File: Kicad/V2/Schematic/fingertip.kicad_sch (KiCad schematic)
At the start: 1 part

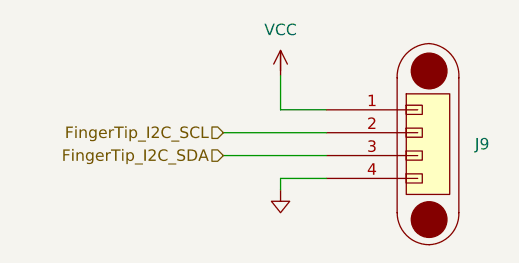
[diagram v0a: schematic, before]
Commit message: New footprints : Ferrite bead, poly fuse, TVS diode. To do: FPC connector footprint
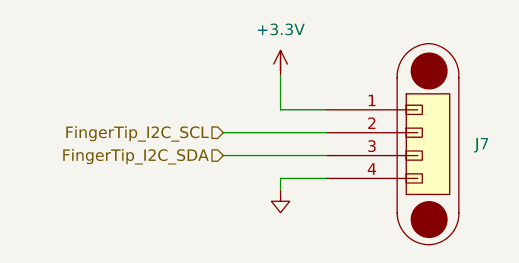
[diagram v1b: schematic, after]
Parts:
- renumbered J9 to J7
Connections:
- net VCC renamed +3.3V
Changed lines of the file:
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@@
 		(dnp no)
 		(fields_autoplaced yes)
-		(property "Reference" "GND039"
+		(property "Reference" "GND041"
 			(at 130.81 100.076 0)
 			(hide yes)
@@
 			(project "G-Love"
 				(path "/808bc5ea-49ac-4454-ba77-8b20d01ce159/8701d982-557e-4c73-bfaa-5f02d2e6c25d"
-					(reference "GND039")
+					(reference "GND041")
+					(unit 1)
+				)
+			)
+		)
+	)
+	(symbol
+		(lib_id "G-Love:+3.3V")
+		(at 130.81 82.55 0)
+		(unit 1)
+		(body_style 1)
+		(exclude_from_sim no)
+		(in_bom no)
+		(on_board no)
+		(in_pos_files yes)
+		(dnp no)
+		(fields_autoplaced yes)
+		(property "Reference" "#PWR024"
+			(at 134.62 84.328 0)
+			(hide yes)
+			(show_name no)
+			(do_not_autoplace no)
+			(effects
+				(font
+					(size 1.27 1.27)
+				)
+			)
+		)
+		(property "Value" "+3.3V"
+			(at 130.81 78.74 0)
+			(show_name no)
+			(do_not_autoplace no)
+			(effects
+				(font
+					(size 1.27 1.27)
+				)
+			)
+		)
+		(property "Footprint" ""
+			(at 130.81 82.55 0)
+			(hide yes)
+			(show_name no)
+			(do_not_autoplace no)
+			(effects
+				(font
+					(size 1.27 1.27)
+				)
+			)
+		)
+		(property "Datasheet" ""
+			(at 130.81 82.55 0)
+			(hide yes)
+			(show_name no)
+			(do_not_autoplace no)
+			(effects
+				(font
+					(size 1.27 1.27)
+				)
+			)
+		)
+		(property "Description" ""
+			(at 130.81 82.55 0)
+			(hide yes)
+			(show_name no)
+			(do_not_autoplace no)
+			(effects
+				(font
+					(size 1.27 1.27)
+				)
+			)
+		)
+		(pin "1"
+		)
+		(instances
+			(project "G-Love"
+				(path "/808bc5ea-49ac-4454-ba77-8b20d01ce159/8701d982-557e-4c73-bfaa-5f02d2e6c25d"
+					(reference "#PWR024")
 					(unit 1)
 				)
@@
 		(dnp no)
 		(fields_autoplaced yes)
-		(property "Reference" "J9"
+		(property "Reference" "J7"
 			(at 152.4 91.4399 0)
 			(show_name no)
@@
 			(project "G-Love"
 				(path "/808bc5ea-49ac-4454-ba77-8b20d01ce159/8701d982-557e-4c73-bfaa-5f02d2e6c25d"
-					(reference "J9")
+					(reference "J7")
 					(unit 1)
 				)
-			)
-		)
-	)
-	(symbol
-		(lib_id "G-Love:VCC")
-		(at 130.81 82.55 0)
-		(unit 1)
-		(body_style 1)
-		(exclude_from_sim no)
-		(in_bom no)
-		(on_board no)
-		(in_pos_files yes)
-		(dnp no)
-		(fields_autoplaced yes)
-		(property "Reference" "#PWR026"
-			(at 134.62 84.328 0)
-			(hide yes)
-			(show_name no)
-			(do_not_autoplace no)
-			(effects
-				(font
-					(size 1.27 1.27)
-				)
-			)
-		)
-		(property "Value" "VCC"
-			(at 130.81 78.74 0)
-			(show_name no)
-			(do_not_autoplace no)
-			(effects
-				(font
-					(size 1.27 1.27)
-				)
-			)
-		)
-		(property "Footprint" ""
-			(at 130.81 82.55 0)
-			(hide yes)
-			(show_name no)
-			(do_not_autoplace no)
-			(effects
-				(font
-					(size 1.27 1.27)
-				)
-			)
-		)
-		(property "Datasheet" ""
-			(at 130.81 82.55 0)
-			(hide yes)
-			(show_name no)
-			(do_not_autoplace no)
-			(effects
-				(font
-					(size 1.27 1.27)
-				)
-			)
-		)
-		(property "Description" ""
-			(at 130.81 82.55 0)
-			(hide yes)
-			(show_name no)
-			(do_not_autoplace no)
-			(effects
-				(font
-					(size 1.27 1.27)
-				)
-			)
-		)
-		(pin "1"
-		)
-		(instances
-			(project "G-Love"
-				(path "/808bc5ea-49ac-4454-ba77-8b20d01ce159/8701d982-557e-4c73-bfaa-5f02d2e6c25d"
-					(reference "#PWR026")
-					(unit 1)
-				)
